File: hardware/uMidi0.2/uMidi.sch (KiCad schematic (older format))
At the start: 55 parts, among them CON1 USB-MINI-B, IC1 6N138, IC2 ATXMEGA128A4U-M, P1 MIDI In, P2 MIDI Thru, P3 MIDI T/O, P4 MIDI Out, P5 5..12 V, P6 PDI, P7 GPIO1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

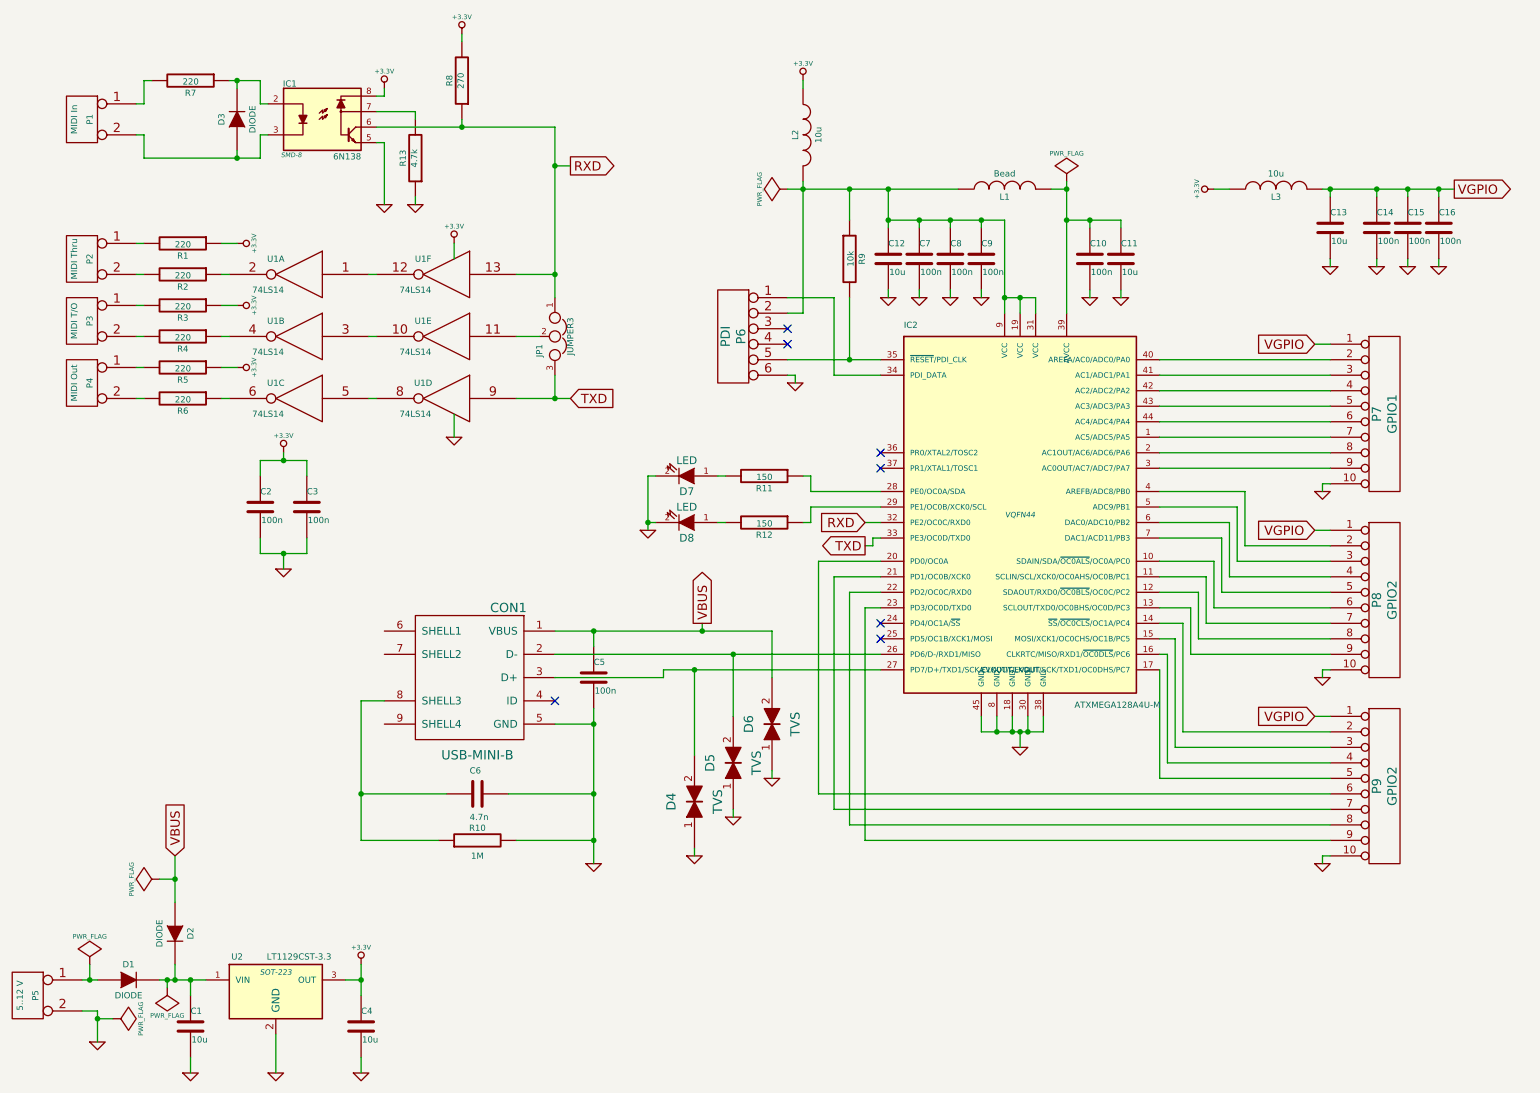
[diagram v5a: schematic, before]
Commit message: Standardize IC names
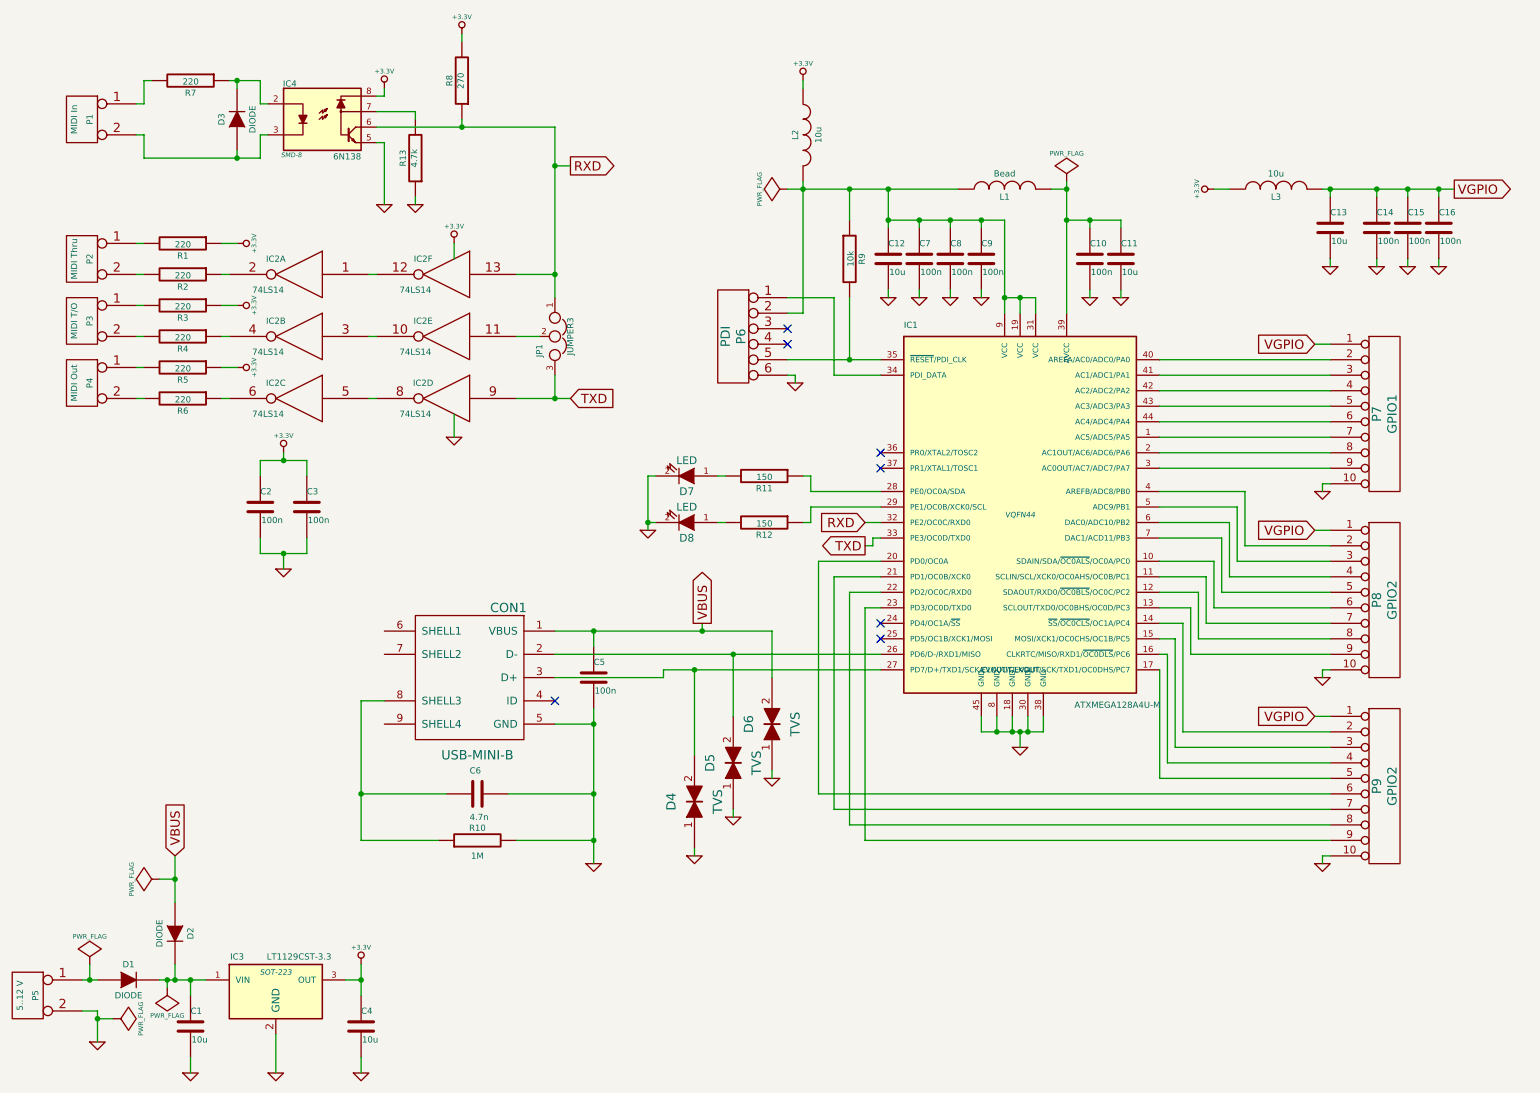
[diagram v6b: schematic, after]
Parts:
- renumbered IC2 to IC1, U1 to IC2, U2 to IC3, IC1 to IC4
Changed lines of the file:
@@
 $EndDescr
 $Comp
-L ATXMEGA128A4U-M IC2
+L ATXMEGA128A4U-M IC1
 U 1 1 53C6C32C
 P 7200 3750
-F 0 "IC2" H 6450 4950 40  0000 L BNN
+F 0 "IC1" H 6450 4950 40  0000 L BNN
 F 1 "ATXMEGA128A4U-M" H 7550 2500 40  0000 L BNN
 F 2 "VQFN44" H 7200 3750 35  0000 C CIN
@@
 $EndComp
 $Comp
-L 74LS14 U1
+L 74LS14 IC2
 U 4 1 53C6D4D0
 P 3500 3000
-F 0 "U1" H 3650 3100 40  0000 C CNN
+F 0 "IC2" H 3650 3100 40  0000 C CNN
 F 1 "74LS14" H 3700 2900 40  0000 C CNN
 F 2 "" H 3500 3000 60  0000 C CNN
@@
 $EndComp
 $Comp
-L 74LS14 U1
+L 74LS14 IC2
 U 1 1 53C6D4E4
 P 2550 2200
-F 0 "U1" H 2700 2300 40  0000 C CNN
+F 0 "IC2" H 2700 2300 40  0000 C CNN
 F 1 "74LS14" H 2750 2100 40  0000 C CNN
 F 2 "" H 2550 2200 60  0000 C CNN
@@
 $EndComp
 $Comp
-L 74LS14 U1
+L 74LS14 IC2
 U 2 1 53C6D4F8
 P 2550 2600
-F 0 "U1" H 2700 2700 40  0000 C CNN
+F 0 "IC2" H 2700 2700 40  0000 C CNN
 F 1 "74LS14" H 2750 2500 40  0000 C CNN
 F 2 "" H 2550 2600 60  0000 C CNN
@@
 $EndComp
 $Comp
-L 74LS14 U1
+L 74LS14 IC2
 U 5 1 53C6D50C
 P 3500 2600
-F 0 "U1" H 3650 2700 40  0000 C CNN
+F 0 "IC2" H 3650 2700 40  0000 C CNN
 F 1 "74LS14" H 3700 2500 40  0000 C CNN
 F 2 "" H 3500 2600 60  0000 C CNN
@@
 $EndComp
 $Comp
-L 74LS14 U1
+L 74LS14 IC2
 U 6 1 53C6D520
 P 3500 2200
-F 0 "U1" H 3650 2300 40  0000 C CNN
+F 0 "IC2" H 3650 2300 40  0000 C CNN
 F 1 "74LS14" H 3700 2100 40  0000 C CNN
 F 2 "" H 3500 2200 60  0000 C CNN
@@
 $EndComp
 $Comp
-L 74LS14 U1
+L 74LS14 IC2
 U 3 1 53C6D534
 P 2550 3000
-F 0 "U1" H 2700 3100 40  0000 C CNN
+F 0 "IC2" H 2700 3100 40  0000 C CNN
 F 1 "74LS14" H 2750 2900 40  0000 C CNN
 F 2 "" H 2550 3000 60  0000 C CNN
@@
 $EndComp
 $Comp
-L 6N135 IC1
+L 6N135 IC4
 U 1 1 53C94FAA
 P 2700 1200
-F 0 "IC1" H 2490 1430 40  0000 C CNN
+F 0 "IC4" H 2490 1430 40  0000 C CNN
 F 1 "6N138" H 2860 960 40  0000 C CNN
 F 2 "SMD-8" H 2500 970 30  0000 C CIN
@@
 $EndComp
 $Comp
-L LT1129CST-3.3 U2
+L LT1129CST-3.3 IC3
 U 1 1 53CAB726
 P 2400 6800
-F 0 "U2" H 2150 7000 40  0000 C CNN
+F 0 "IC3" H 2150 7000 40  0000 C CNN
 F 1 "LT1129CST-3.3" H 2550 7000 40  0000 C CNN
 F 2 "SOT-223" H 2400 6900 35  0000 C CIN

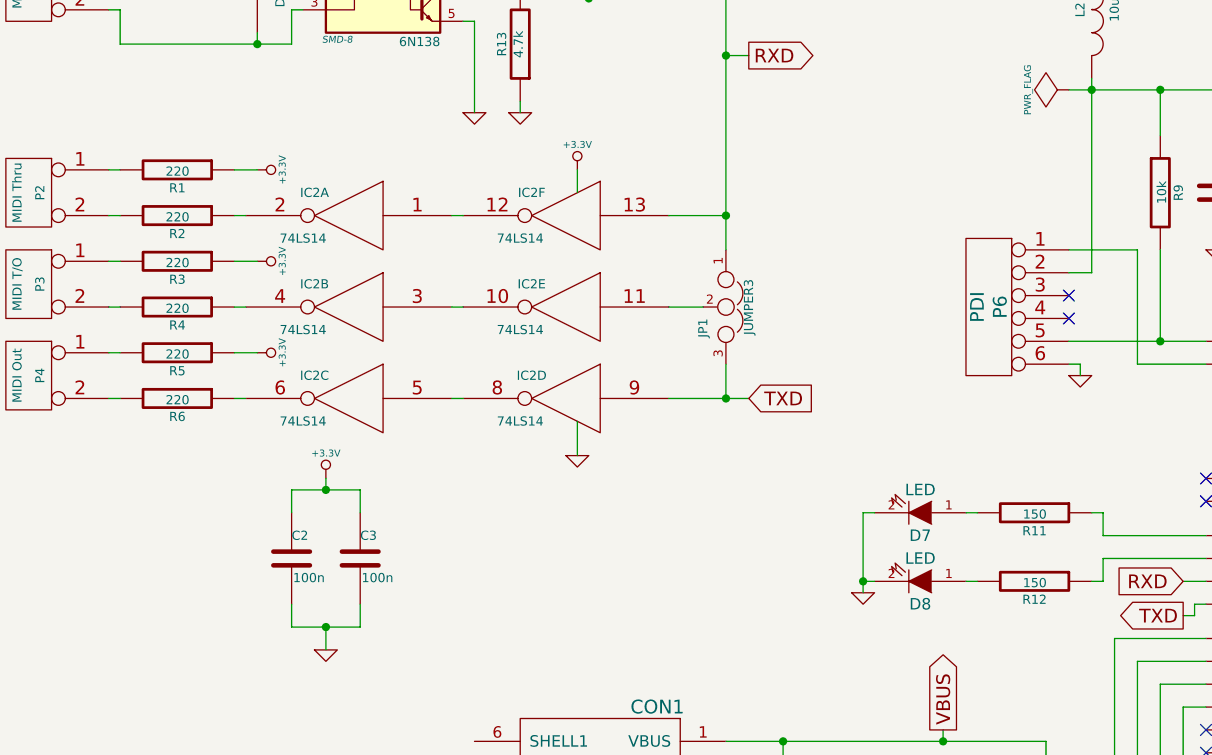
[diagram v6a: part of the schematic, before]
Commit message: Revise resistor dimensioning
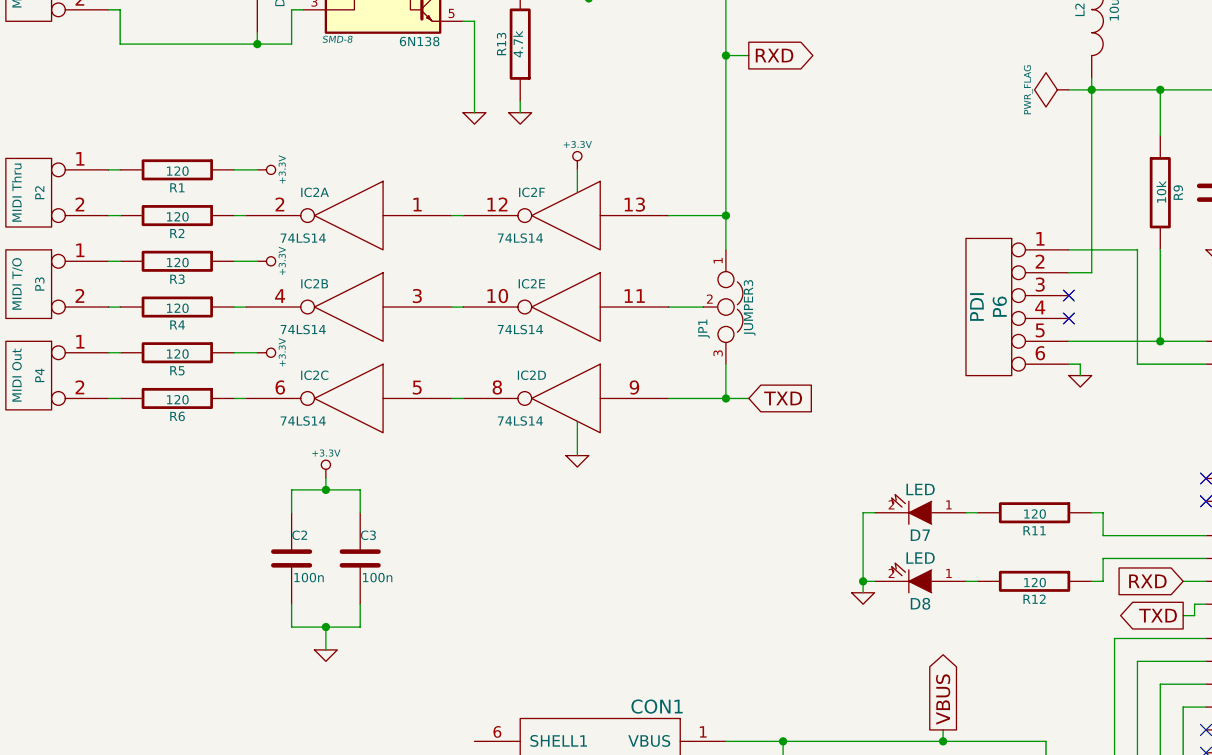
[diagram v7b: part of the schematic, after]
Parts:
- R1, R2, R3, R4, R5, R6: value 220 -> 120
- R11, R12: value 150 -> 120
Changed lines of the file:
@@
 P 1800 2200
 F 0 "R2" V 1880 2200 40  0000 C CNN
-F 1 "220" V 1807 2201 40  0000 C CNN
+F 1 "120" V 1807 2201 40  0000 C CNN
 F 2 "" V 1730 2200 30  0000 C CNN
 F 3 "" H 1800 2200 30  0000 C CNN
@@
 P 1800 2600
 F 0 "R4" V 1880 2600 40  0000 C CNN
-F 1 "220" V 1807 2601 40  0000 C CNN
+F 1 "120" V 1807 2601 40  0000 C CNN
 F 2 "" V 1730 2600 30  0000 C CNN
 F 3 "" H 1800 2600 30  0000 C CNN
@@
 P 1800 3000
 F 0 "R6" V 1880 3000 40  0000 C CNN
-F 1 "220" V 1807 3001 40  0000 C CNN
+F 1 "120" V 1807 3001 40  0000 C CNN
 F 2 "" V 1730 3000 30  0000 C CNN
 F 3 "" H 1800 3000 30  0000 C CNN
@@
 P 1800 2000
 F 0 "R1" V 1880 2000 40  0000 C CNN
-F 1 "220" V 1807 2001 40  0000 C CNN
+F 1 "120" V 1807 2001 40  0000 C CNN
 F 2 "" V 1730 2000 30  0000 C CNN
 F 3 "" H 1800 2000 30  0000 C CNN
@@
 P 1800 2400
 F 0 "R3" V 1880 2400 40  0000 C CNN
-F 1 "220" V 1807 2401 40  0000 C CNN
+F 1 "120" V 1807 2401 40  0000 C CNN
 F 2 "" V 1730 2400 30  0000 C CNN
 F 3 "" H 1800 2400 30  0000 C CNN
@@
 P 1800 2800
 F 0 "R5" V 1880 2800 40  0000 C CNN
-F 1 "220" V 1807 2801 40  0000 C CNN
+F 1 "120" V 1807 2801 40  0000 C CNN
 F 2 "" V 1730 2800 30  0000 C CNN
 F 3 "" H 1800 2800 30  0000 C CNN
@@
 P 5550 3500
 F 0 "R11" V 5630 3500 40  0000 C CNN
-F 1 "150" V 5557 3501 40  0000 C CNN
+F 1 "120" V 5557 3501 40  0000 C CNN
 F 2 "" V 5480 3500 30  0000 C CNN
 F 3 "" H 5550 3500 30  0000 C CNN
@@
 P 5550 3800
 F 0 "R12" V 5630 3800 40  0000 C CNN
-F 1 "150" V 5557 3801 40  0000 C CNN
+F 1 "120" V 5557 3801 40  0000 C CNN
 F 2 "" V 5480 3800 30  0000 C CNN
 F 3 "" H 5550 3800 30  0000 C CNN
